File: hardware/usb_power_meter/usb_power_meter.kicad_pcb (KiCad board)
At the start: 4 copper layers, 35.3 x 19.6 mm, 22 parts, among them U1 nRF52833-QDxx, U2 INA226, X1 32Mhz crystal, X2 32.768kHz crystal

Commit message: Add debugging connector
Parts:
- added J1: Conn_ARM_JTAG_SWD_10, Connector_PinHeader_1.27mm:PinHeader_2x05_P1.27mm_Vertical_SMD, F.Cu at (122.7, 110.9)
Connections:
- U1 pad 16: unconnected-(U1-P0.18/~{RESET}-Pad16) -> Net-(J1-~{RESET})
- U1 pad 19: unconnected-(U1-SWDIO-Pad19) -> Net-(J1-SWDIO/TMS)
- U1 pad 20: unconnected-(U1-SWDCLK-Pad20) -> Net-(J1-SWDCLK/TCK)
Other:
- board size 35.3 x 19.6 mm -> 33 x 24.6 mm

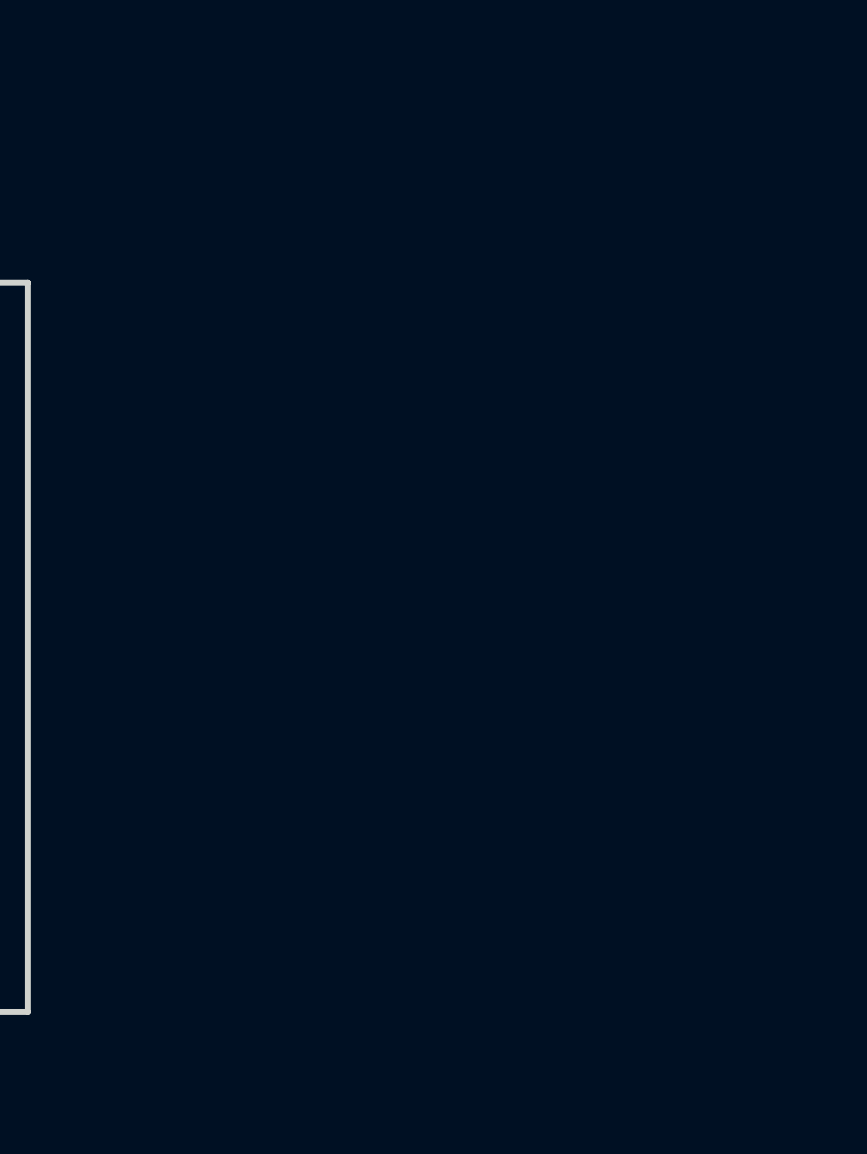
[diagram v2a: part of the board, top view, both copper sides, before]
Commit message: Add most of the components. Some TODOs still remain.
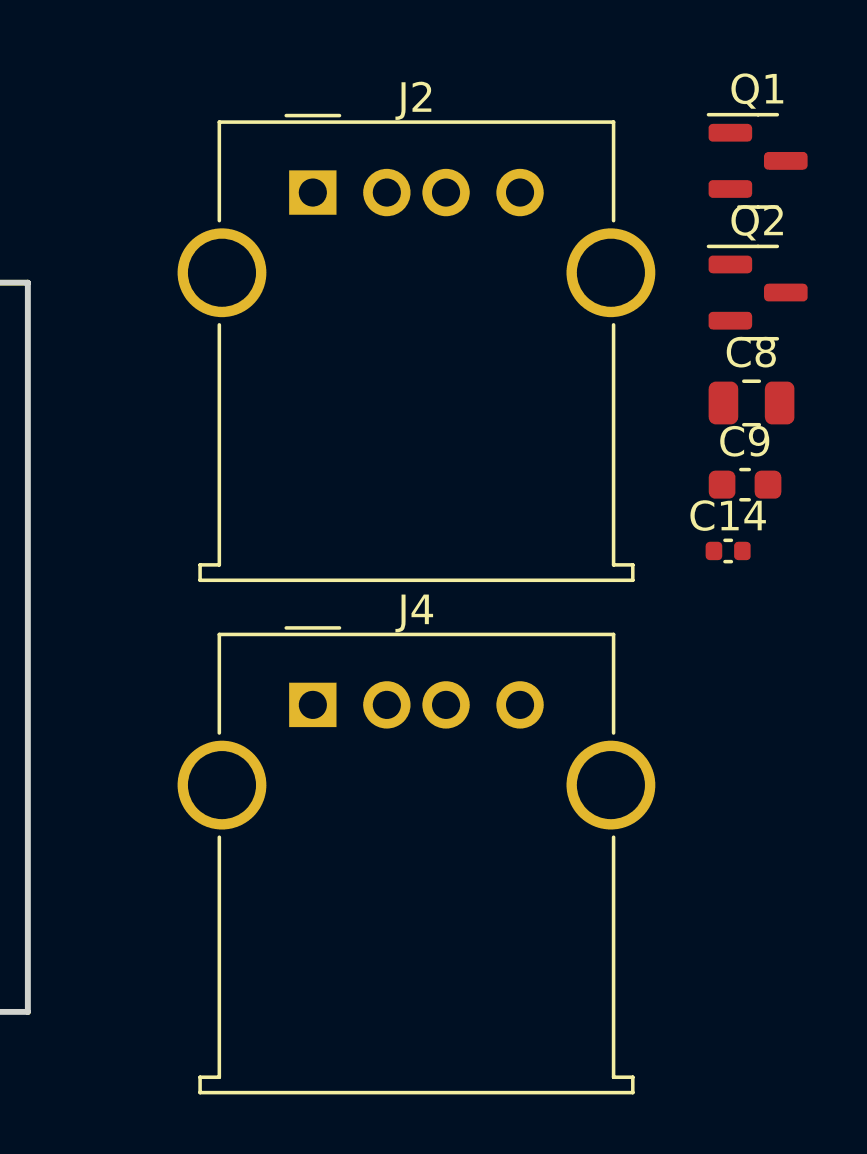
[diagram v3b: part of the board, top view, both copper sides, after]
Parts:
- added C14: 100 nF, Capacitor_SMD:C_0402_1005Metric, F.Cu at (175.0, 100.2)
- added C8: 10 uF, Capacitor_SMD:C_0805_2012Metric, F.Cu at (175.8, 95.2)
- added C9: 10 nF, Capacitor_SMD:C_0603_1608Metric, F.Cu at (175.6, 98.0)
- added J2: USB_A, Connector_USB:USB_A_Molex_67643_Horizontal, F.Cu at (161.0, 88.1)
- added J4: USB_A, Connector_USB:USB_A_Molex_67643_Horizontal, F.Cu at (161.0, 105.5)
- added Q1: 2N7002, Package_TO_SOT_SMD:SOT-23, F.Cu at (176.1, 87.1)
- added Q2: IRML6401, Package_TO_SOT_SMD:SOT-23, F.Cu at (176.1, 91.5)
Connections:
- U1 pad 14: unconnected-(U1-P0.15-Pad14) -> /EN_PWR
- U2 pad 6: unconnected-(U2-VS-Pad6) -> VBUS
- U2 pad 8: unconnected-(U2-Vbus-Pad8) -> VBUS

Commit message: Draft routing done
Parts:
- added C18: 100 nF, Capacitor_SMD:C_0402_1005Metric, F.Cu at (118.6, 102.6)
- added R2: 10k, Resistor_SMD:R_0201_0603Metric, F.Cu at (118.9, 112.1)
- added R3: 10k, Resistor_SMD:R_0201_0603Metric, F.Cu at (130.6, 108.7)
- added R5: 10k, Resistor_SMD:R_0201_0603Metric, F.Cu at (129.0, 100.8)
- added R6: 10k, Resistor_SMD:R_0201_0603Metric, F.Cu at (129.2, 101.7)
- added R7: 10k, Resistor_SMD:R_0201_0603Metric, F.Cu at (129.2, 102.6)
- added R8: LRP12FTDSR020, Resistor_SMD:R_2512_6332Metric, F.Cu at (121.8, 108.5)
- moved Q2 58.8 mm to (121.4, 113.2), turned to -90 degrees
- moved C8 57.5 mm to (118.4, 97.5), turned to 90 degrees
- moved Q1 55.8 mm to (126.7, 113.3), turned to 90 degrees
- moved C9 55.5 mm to (120.1, 97.3), turned to 90 degrees
- moved C14 53.7 mm to (121.4, 96.8), turned to 90 degrees
- moved J2 48.3 mm to (114.0, 99.4), turned to -90 degrees
- moved J4 45.2 mm to (118.0, 119.5)
- moved J1 24.4 mm to (143.0, 124.5), turned to 90 degrees
- moved R1 10.8 mm to (121.9, 98.3)
- moved C1 2.79 mm to (138.0, 98.8), turned to -90 degrees
- moved C5 1.01 mm to (128.4, 97.3)
- moved C19 0.25 mm to (132.1, 108.0)
- turned C2 to 0 degrees
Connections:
- Q2 pad 2: VBUS -> Net-(Q2-S)
- U2 pad 10: unconnected-(U2-Vin+-Pad10) -> VBUS
- U2 pad 9: unconnected-(U2-Vin--Pad9) -> Net-(Q2-S)
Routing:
- net VDD: track 0.00 -> 59.4 mm, vias 0 -> 8
- net GND: track 0.00 -> 35.5 mm, vias 0 -> 2
- net VBUS: track 0.00 -> 25.4 mm
- net Net-(J1-~{RESET}): track 0.00 -> 24.5 mm, vias 0 -> 2
- net Net-(J1-SWDCLK/TCK): track 0.00 -> 19.7 mm
- net Net-(J1-SWDIO/TMS): track 0.00 -> 19.3 mm
- net Net-(U1-VBUS): track 0.00 -> 18.8 mm, vias 0 -> 2
- net /EN_PWR: track 0.00 -> 14.0 mm
- net unconnected-(J2-Shield-Pad5): track 0.00 -> 13.1 mm
- net unconnected-(J4-Shield-Pad5): track 0.00 -> 13.1 mm
- net Net-(Q2-S): track 0.00 -> 11.8 mm
- net Net-(U1-DEC4): track 0.00 -> 11.8 mm, vias 0 -> 2
- net Net-(U1-XL2/P0.01): track 0.00 -> 11.6 mm
- net Net-(Q1-D): track 0.00 -> 8.72 mm
- net Net-(U1-XC1): track 0.00 -> 8.65 mm
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- added copper zone on F.Cu, net GND
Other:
- board size 33 x 24.6 mm -> 39.9 x 39.1 mm

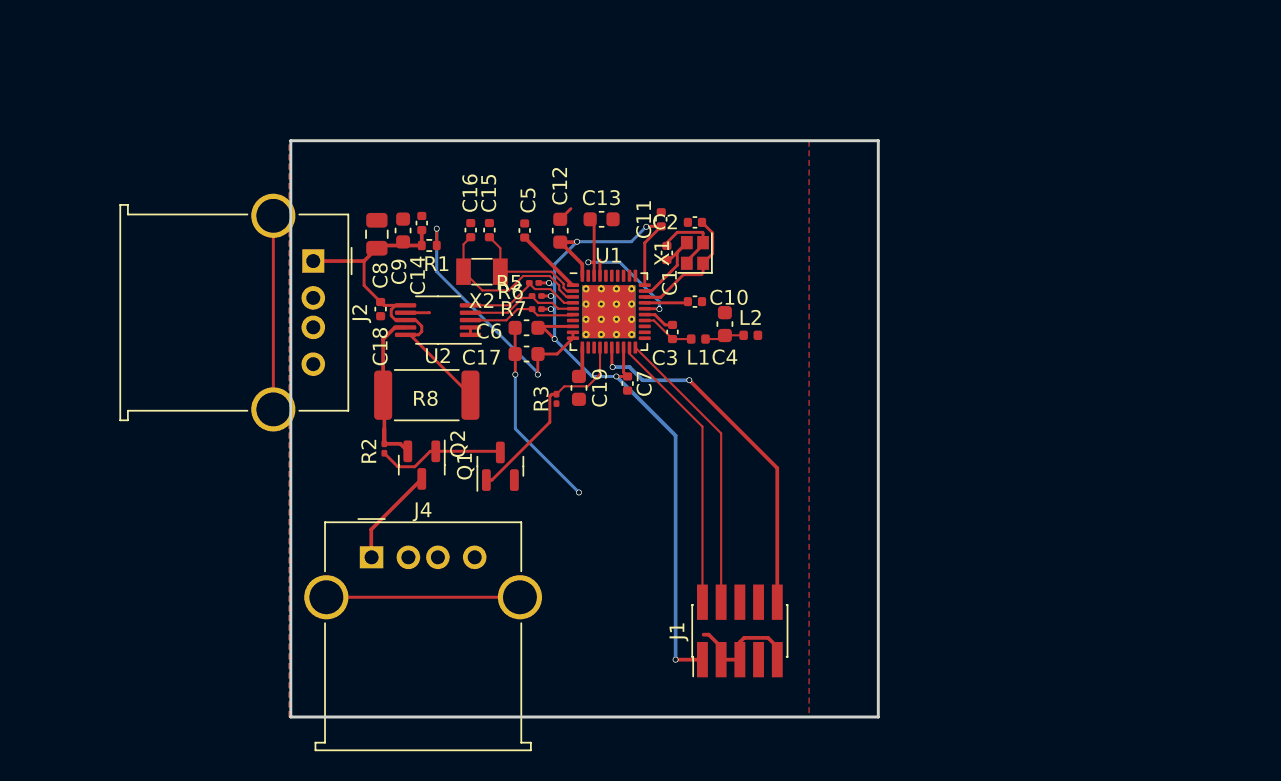
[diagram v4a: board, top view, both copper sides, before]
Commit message: Make board a bit smaller and prepare space for antenna
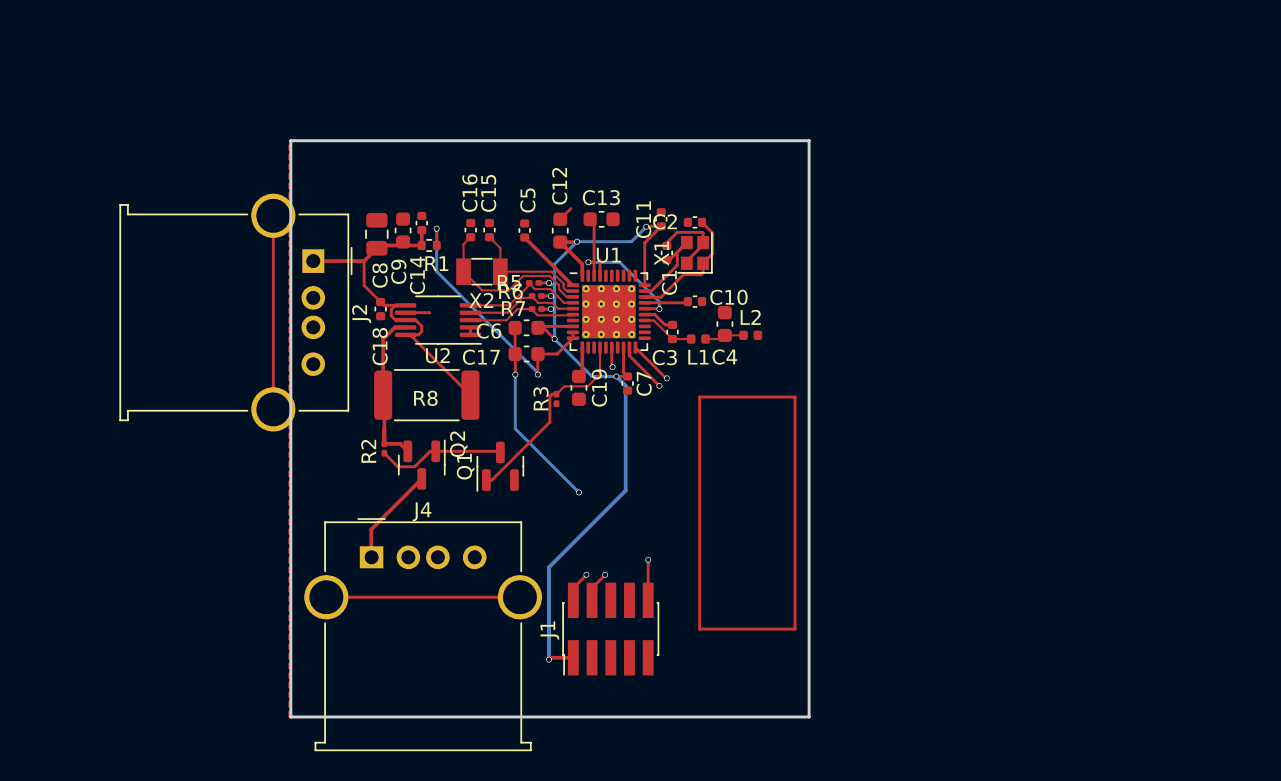
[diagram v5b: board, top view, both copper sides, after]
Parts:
- moved J1 8.76 mm to (134.2, 124.3)
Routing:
- net GND: track 35.5 -> 26.4 mm
- net Net-(J1-~{RESET}): track 24.5 -> 19.3 mm
- net Net-(J1-SWDIO/TMS): track 19.3 -> 22.8 mm, vias 0 -> 2
- net Net-(J1-SWDCLK/TCK): track 19.7 -> 22.4 mm, vias 0 -> 2
- net VDD: track 59.4 -> 60.1 mm
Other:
- board size 39.9 x 39.1 mm -> 35.2 x 39.1 mm

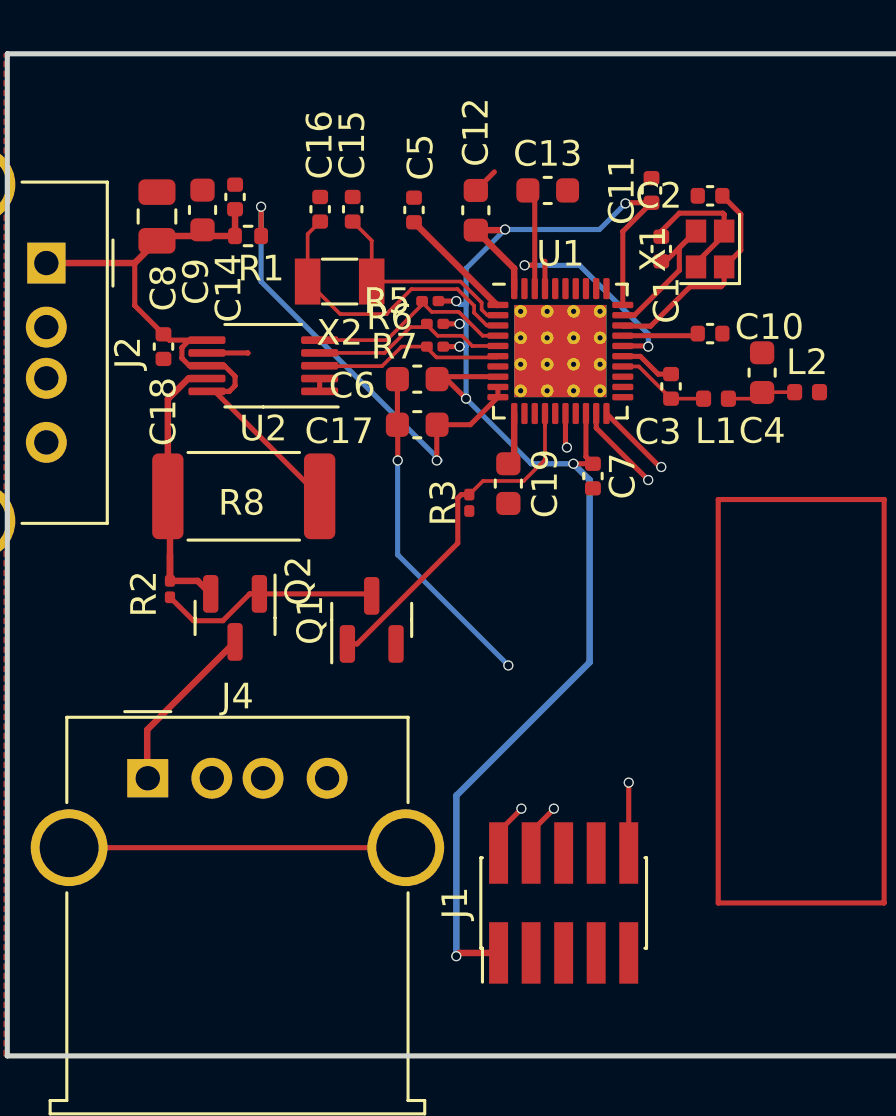
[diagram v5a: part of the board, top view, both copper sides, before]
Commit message: Fix most of DRC violation
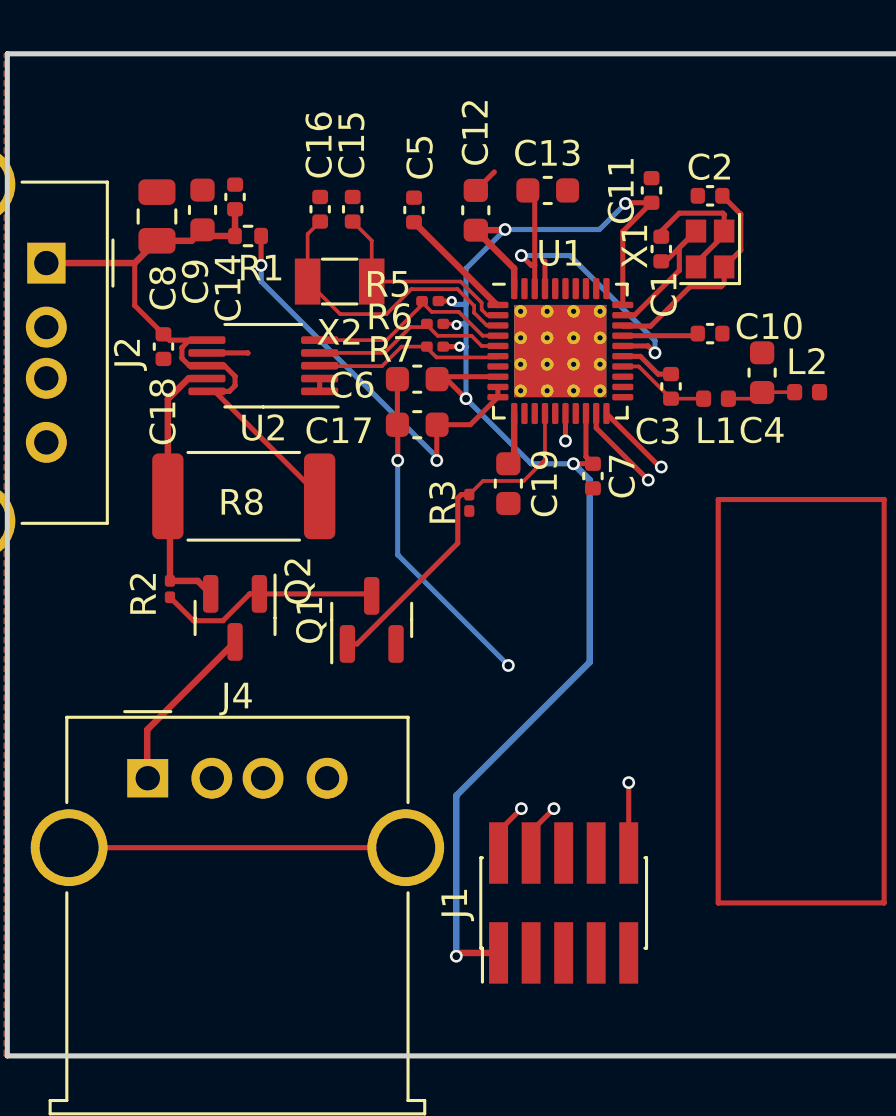
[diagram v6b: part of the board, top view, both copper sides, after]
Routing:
- net Net-(U1-VBUS): track 18.8 -> 16.4 mm
- net Net-(U1-DEC4): track 11.8 -> 13.1 mm
- net Net-(Q2-S): track 11.8 -> 10.8 mm
